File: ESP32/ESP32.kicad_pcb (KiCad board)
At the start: 2 copper layers, 17.8 x 33 mm, 20 parts, among them J1 USB_C_Receptacle_USB2.0, J2 Conn_Coaxial, U1 ESP32-PICO-D4, U2 W25Q32JVZP, U3 CP2104, U4 AP2112K-3.3

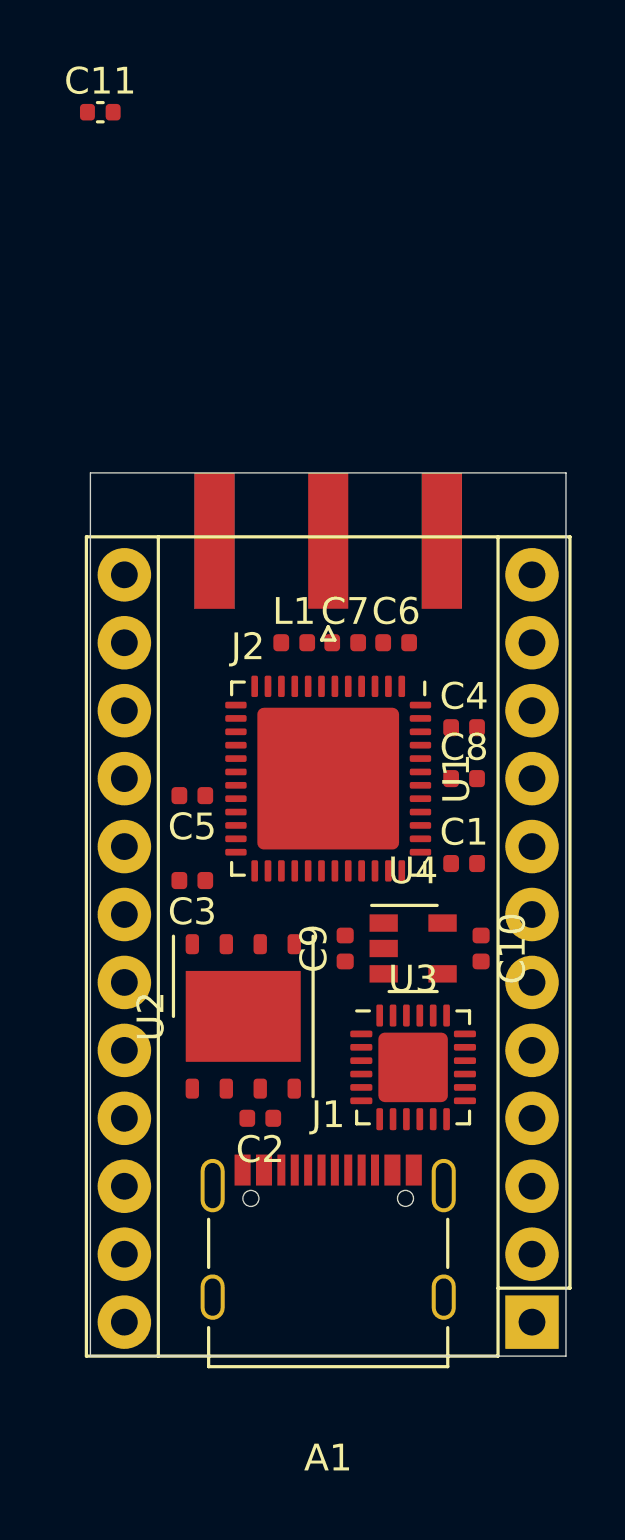
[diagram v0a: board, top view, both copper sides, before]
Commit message: make controller holes wide enough
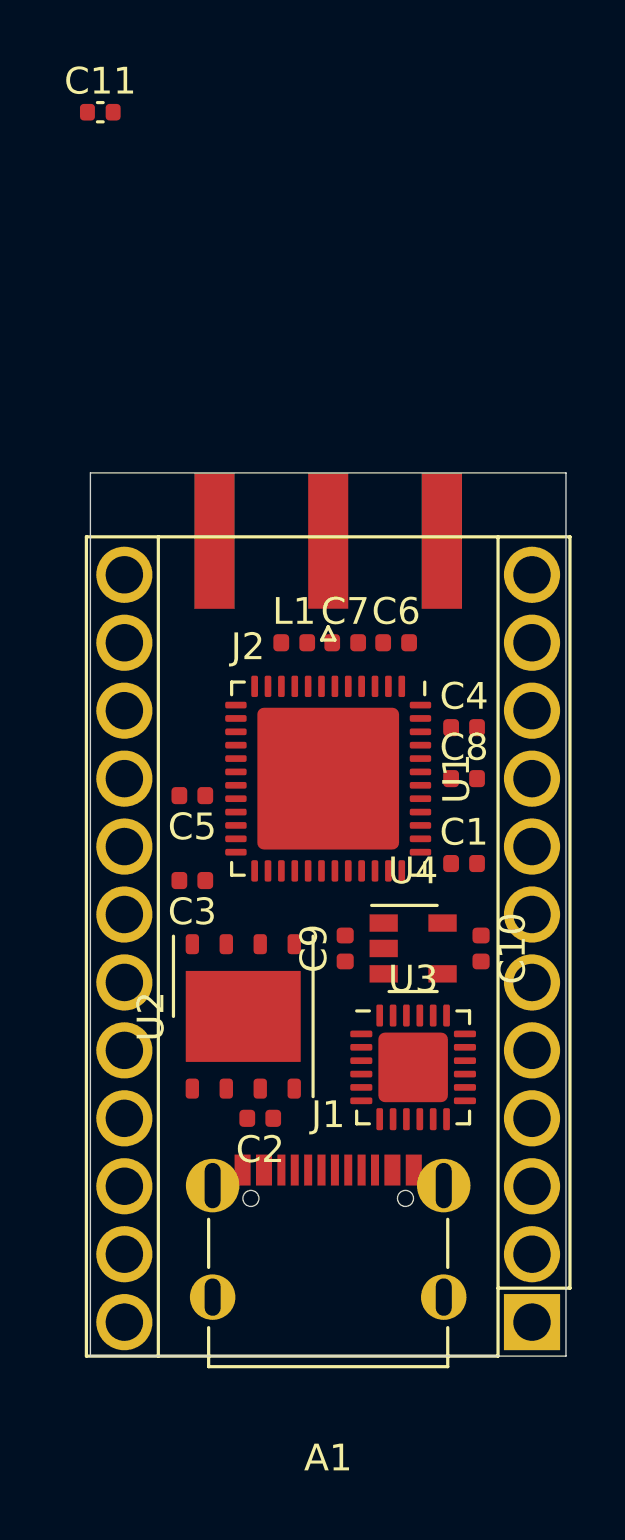
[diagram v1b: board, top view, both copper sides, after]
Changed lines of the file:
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@@
-(kicad_pcb (version 20171130) (host pcbnew 5.1.5+dfsg1-2build2)
+(kicad_pcb (version 20171130) (host pcbnew 5.1.5)
   (general
     (thickness 1.6)
@@
     (pad B7 smd rect (at -0.75 -2.51 180) (size 0.3 1.16) (layers F.Cu F.Paste F.Mask)
       (net 5 /D-))
-    (pad S1 thru_hole oval (at 4.32 2.24 90) (size 1.7 0.9) (drill oval 1.4 0.6) (layers *.Cu *.Mask)
-      (net 1 GND))
-    (pad S1 thru_hole oval (at -4.32 2.24 90) (size 1.7 0.9) (drill oval 1.4 0.6) (layers *.Cu *.Mask)
-      (net 1 GND))
-    (pad S1 thru_hole oval (at 4.32 -1.93 90) (size 2 0.9) (drill oval 1.7 0.6) (layers *.Cu *.Mask)
-      (net 1 GND))
-    (pad S1 thru_hole oval (at -4.32 -1.93 90) (size 2 0.9) (drill oval 1.7 0.6) (layers *.Cu *.Mask)
+    (pad S1 thru_hole circle (at 4.32 2.24 90) (size 1.7 0.9) (drill oval 1.4 0.6) (layers *.Cu *.Mask)
+      (net 1 GND))
+    (pad S1 thru_hole circle (at -4.32 2.24 90) (size 1.7 0.9) (drill oval 1.4 0.6) (layers *.Cu *.Mask)
+      (net 1 GND))
+    (pad S1 thru_hole circle (at 4.32 -1.93 90) (size 2 0.9) (drill oval 1.7 0.6) (layers *.Cu *.Mask)
+      (net 1 GND))
+    (pad S1 thru_hole circle (at -4.32 -1.93 90) (size 2 0.9) (drill oval 1.7 0.6) (layers *.Cu *.Mask)
       (net 1 GND))
     (model ${KISYS3DMOD}/Connector_USB.3dshapes/USB_C_Receptacle_Palconn_UTC16-G.wrl
@@
       (effects (font (size 1 1) (thickness 0.15)))
     )
-    (pad 1 thru_hole rect (at 0 0 180) (size 2 2) (drill 1) (layers *.Cu *.Mask)
+    (pad 1 thru_hole rect (at 0 0 180) (size 2.1 2.1) (drill 1.4) (layers *.Cu *.Mask)
       (net 19 RXD))
-    (pad 2 thru_hole oval (at 0 2.54 180) (size 2 2) (drill 1) (layers *.Cu *.Mask)
+    (pad 2 thru_hole circle (at 0 2.54 180) (size 2.1 2.1) (drill 1.4) (layers *.Cu *.Mask)
       (net 20 TXD))
-    (pad 3 thru_hole oval (at 0 5.08 180) (size 2 2) (drill 1) (layers *.Cu *.Mask)
-      (net 1 GND))
-    (pad 13 thru_hole oval (at 15.24 27.94 180) (size 2 2) (drill 1) (layers *.Cu *.Mask))
-    (pad 4 thru_hole oval (at 0 7.62 180) (size 2 2) (drill 1) (layers *.Cu *.Mask)
-      (net 1 GND))
-    (pad 14 thru_hole oval (at 15.24 25.4 180) (size 2 2) (drill 1) (layers *.Cu *.Mask))
-    (pad 5 thru_hole oval (at 0 10.16 180) (size 2 2) (drill 1) (layers *.Cu *.Mask))
-    (pad 15 thru_hole oval (at 15.24 22.86 180) (size 2 2) (drill 1) (layers *.Cu *.Mask))
-    (pad 6 thru_hole oval (at 0 12.7 180) (size 2 2) (drill 1) (layers *.Cu *.Mask))
-    (pad 16 thru_hole oval (at 15.24 20.32 180) (size 2 2) (drill 1) (layers *.Cu *.Mask))
-    (pad 7 thru_hole oval (at 0 15.24 180) (size 2 2) (drill 1) (layers *.Cu *.Mask))
-    (pad 17 thru_hole oval (at 15.24 17.78 180) (size 2 2) (drill 1) (layers *.Cu *.Mask)
+    (pad 3 thru_hole circle (at 0 5.08 180) (size 2.1 2.1) (drill 1.4) (layers *.Cu *.Mask)
+      (net 1 GND))
+    (pad 13 thru_hole circle (at 15.24 27.94 180) (size 2.1 2.1) (drill 1.4) (layers *.Cu *.Mask))
+    (pad 4 thru_hole circle (at 0 7.62 180) (size 2.1 2.1) (drill 1.4) (layers *.Cu *.Mask)
+      (net 1 GND))
+    (pad 14 thru_hole circle (at 15.24 25.4 180) (size 2.1 2.1) (drill 1.4) (layers *.Cu *.Mask))
+    (pad 5 thru_hole circle (at 0 10.16 180) (size 2.1 2.1) (drill 1.4) (layers *.Cu *.Mask))
+    (pad 15 thru_hole circle (at 15.24 22.86 180) (size 2.1 2.1) (drill 1.4) (layers *.Cu *.Mask))
+    (pad 6 thru_hole circle (at 0 12.7 180) (size 2.1 2.1) (drill 1.4) (layers *.Cu *.Mask))
+    (pad 16 thru_hole circle (at 15.24 20.32 180) (size 2.1 2.1) (drill 1.4) (layers *.Cu *.Mask))
+    (pad 7 thru_hole circle (at 0 15.24 180) (size 2.1 2.1) (drill 1.4) (layers *.Cu *.Mask))
+    (pad 17 thru_hole circle (at 15.24 17.78 180) (size 2.1 2.1) (drill 1.4) (layers *.Cu *.Mask)
       (net 6 TDI))
-    (pad 8 thru_hole oval (at 0 17.78 180) (size 2 2) (drill 1) (layers *.Cu *.Mask))
-    (pad 18 thru_hole oval (at 15.24 15.24 180) (size 2 2) (drill 1) (layers *.Cu *.Mask)
+    (pad 8 thru_hole circle (at 0 17.78 180) (size 2.1 2.1) (drill 1.4) (layers *.Cu *.Mask))
+    (pad 18 thru_hole circle (at 15.24 15.24 180) (size 2.1 2.1) (drill 1.4) (layers *.Cu *.Mask)
       (net 7 TDO))
-    (pad 9 thru_hole oval (at 0 20.32 180) (size 2 2) (drill 1) (layers *.Cu *.Mask))
-    (pad 19 thru_hole oval (at 15.24 12.7 180) (size 2 2) (drill 1) (layers *.Cu *.Mask)
+    (pad 9 thru_hole circle (at 0 20.32 180) (size 2.1 2.1) (drill 1.4) (layers *.Cu *.Mask))
+    (pad 19 thru_hole circle (at 15.24 12.7 180) (size 2.1 2.1) (drill 1.4) (layers *.Cu *.Mask)
       (net 8 TMS))
-    (pad 10 thru_hole oval (at 0 22.86 180) (size 2 2) (drill 1) (layers *.Cu *.Mask))
-    (pad 20 thru_hole oval (at 15.24 10.16 180) (size 2 2) (drill 1) (layers *.Cu *.Mask)
+    (pad 10 thru_hole circle (at 0 22.86 180) (size 2.1 2.1) (drill 1.4) (layers *.Cu *.Mask))
+    (pad 20 thru_hole circle (at 15.24 10.16 180) (size 2.1 2.1) (drill 1.4) (layers *.Cu *.Mask)
       (net 9 TCK))
-    (pad 11 thru_hole oval (at 0 25.4 180) (size 2 2) (drill 1) (layers *.Cu *.Mask))
-    (pad 21 thru_hole oval (at 15.24 7.62 180) (size 2 2) (drill 1) (layers *.Cu *.Mask)
-      (net 2 +3V3))
-    (pad 12 thru_hole oval (at 0 27.94 180) (size 2 2) (drill 1) (layers *.Cu *.Mask))
-    (pad 22 thru_hole oval (at 15.24 5.08 180) (size 2 2) (drill 1) (layers *.Cu *.Mask)
+    (pad 11 thru_hole circle (at 0 25.4 180) (size 2.1 2.1) (drill 1.4) (layers *.Cu *.Mask))
+    (pad 21 thru_hole circle (at 15.24 7.62 180) (size 2.1 2.1) (drill 1.4) (layers *.Cu *.Mask)
+      (net 2 +3V3))
+    (pad 12 thru_hole circle (at 0 27.94 180) (size 2.1 2.1) (drill 1.4) (layers *.Cu *.Mask))
+    (pad 22 thru_hole circle (at 15.24 5.08 180) (size 2.1 2.1) (drill 1.4) (layers *.Cu *.Mask)
       (net 21 ~RST))
-    (pad 23 thru_hole oval (at 15.24 2.54 180) (size 2 2) (drill 1) (layers *.Cu *.Mask)
-      (net 1 GND))
-    (pad 24 thru_hole oval (at 15.24 0 180) (size 2 2) (drill 1) (layers *.Cu *.Mask))
+    (pad 23 thru_hole circle (at 15.24 2.54 180) (size 2.1 2.1) (drill 1.4) (layers *.Cu *.Mask)
+      (net 1 GND))
+    (pad 24 thru_hole circle (at 15.24 0 180) (size 2.1 2.1) (drill 1.4) (layers *.Cu *.Mask))
     (model ${KISYS3DMOD}/Module.3dshapes/Sparkfun_Pro_Micro.wrl
       (at (xyz 0 0 0))
